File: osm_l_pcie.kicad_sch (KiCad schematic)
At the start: 1 part, among them U2 OSM-L_Carrier-side

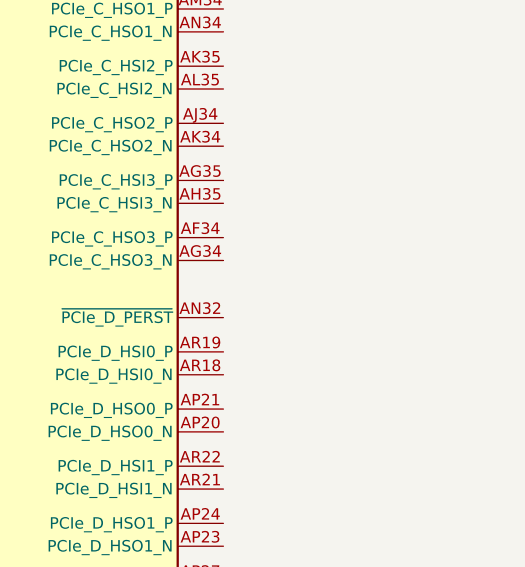
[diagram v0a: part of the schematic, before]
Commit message: [#81876] Add PCIe C&D
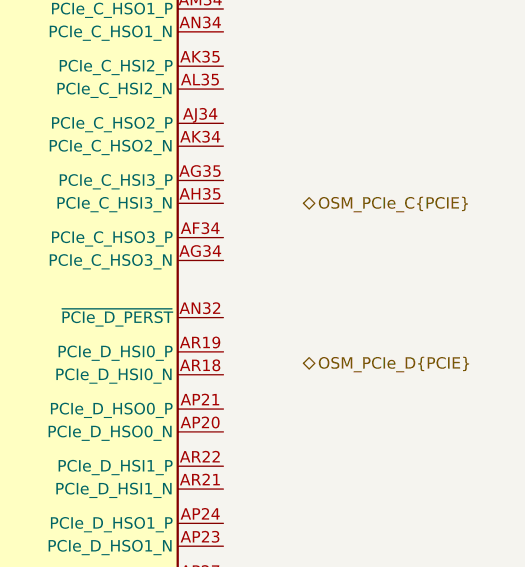
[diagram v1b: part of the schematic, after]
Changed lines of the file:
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@@
+		)
+	)
+	(hierarchical_label "OSM_PCIe_C{PCIE}"
+		(shape bidirectional)
+		(at 330.2 153.67 0)
+		(effects
+			(font
+				(size 1.27 1.27)
+			)
+			(justify left)
+		)
+	)
+	(hierarchical_label "OSM_PCIe_D{PCIE}"
+		(shape bidirectional)
+		(at 330.2 171.45 0)
+		(effects
+			(font
+				(size 1.27 1.27)
+			)
+			(justify left)
 		)
 	)

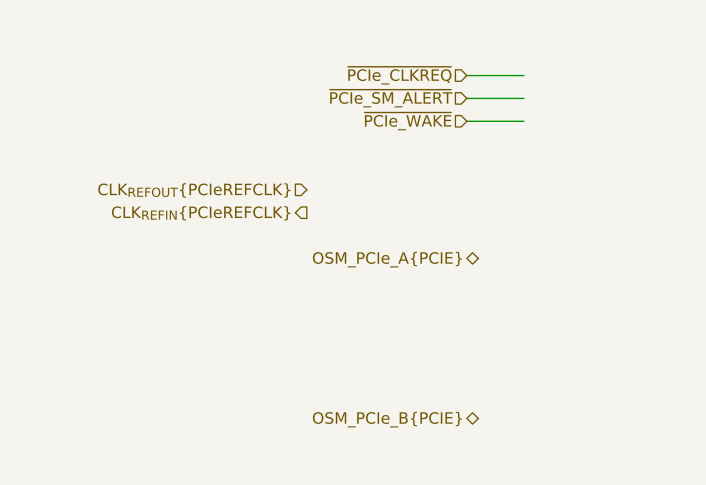
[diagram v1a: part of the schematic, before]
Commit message: [#81876] Continue adding top-level connections
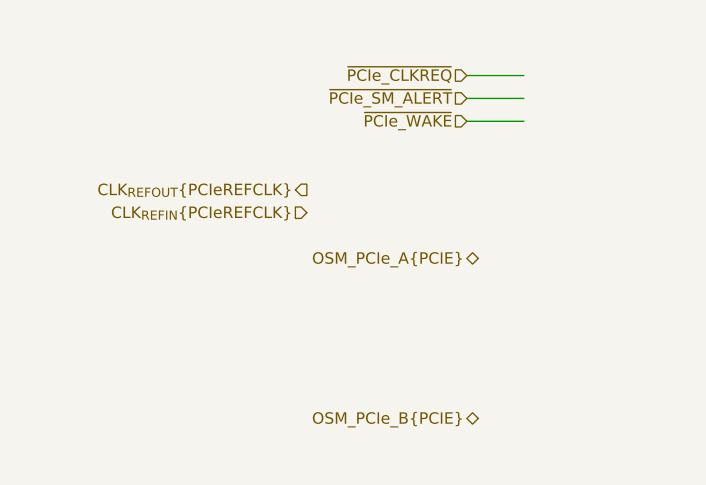
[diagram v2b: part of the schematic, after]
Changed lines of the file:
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@@
 	)
 	(hierarchical_label "CLK_{REFOUT}{PCIeREFCLK}"
-		(shape input)
+		(shape output)
 		(at 158.75 120.65 180)
 		(effects
@@
 	)
 	(hierarchical_label "CLK_{REFIN}{PCIeREFCLK}"
-		(shape output)
+		(shape input)
 		(at 158.75 123.19 180)
 		(effects
